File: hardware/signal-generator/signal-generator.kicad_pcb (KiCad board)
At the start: 2 copper layers, 96.6 x 92.2 mm, 68 parts, among them J1 AVR-ISP-6, J2 Conn_01x04_Male, J3 Power_Supply_Rails, J4 Conn_Coaxial, J5 Conn_01x04, SW1 RESET_BUTTON, SW2 START/STOP, SW3 MODE_SELECT, SW4 UP_ARROW, SW5 DOWN_ARROW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

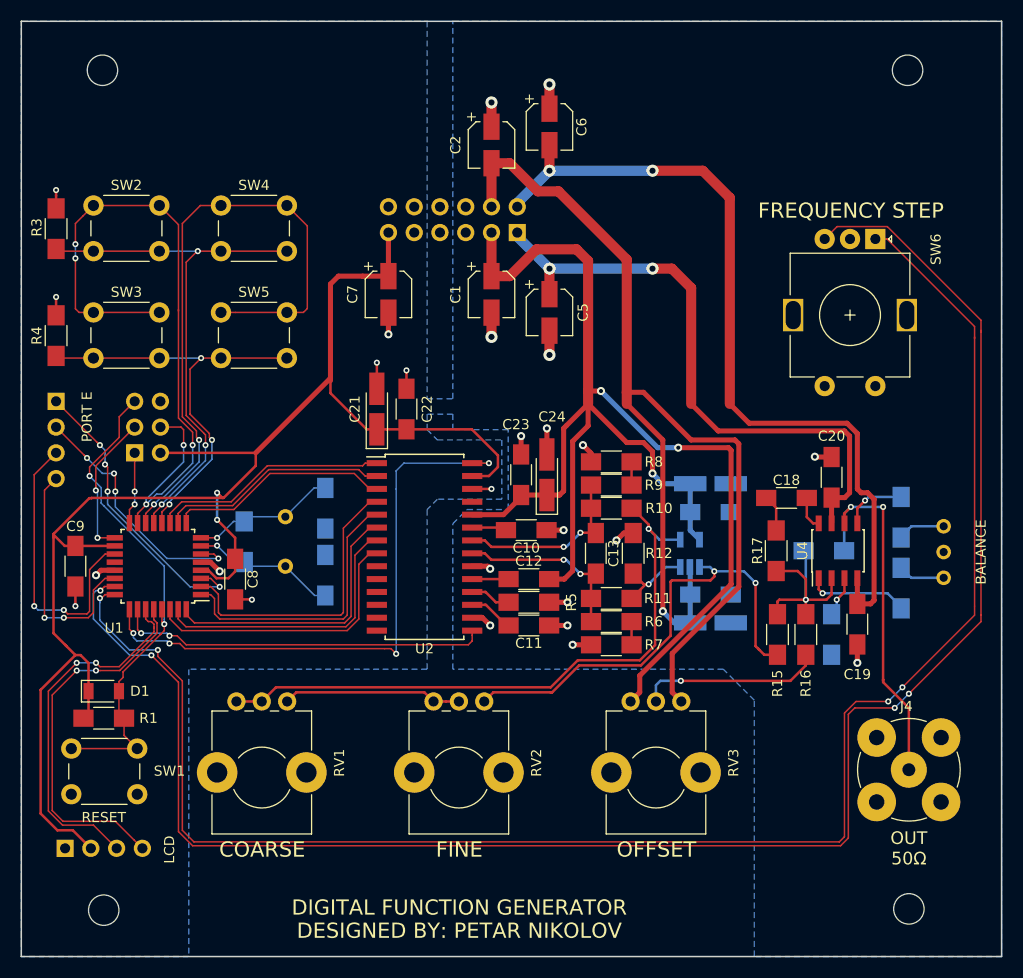
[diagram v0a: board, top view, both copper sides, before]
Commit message: [Signal Generator] Layout new amplifier on PCB
The newer amplifier's components have been placed while following the
AD8021's datasheet recommendations as well as general PCB design
guidelines. However, this is not the final PCB layout: further
fine-tuning may be applied.
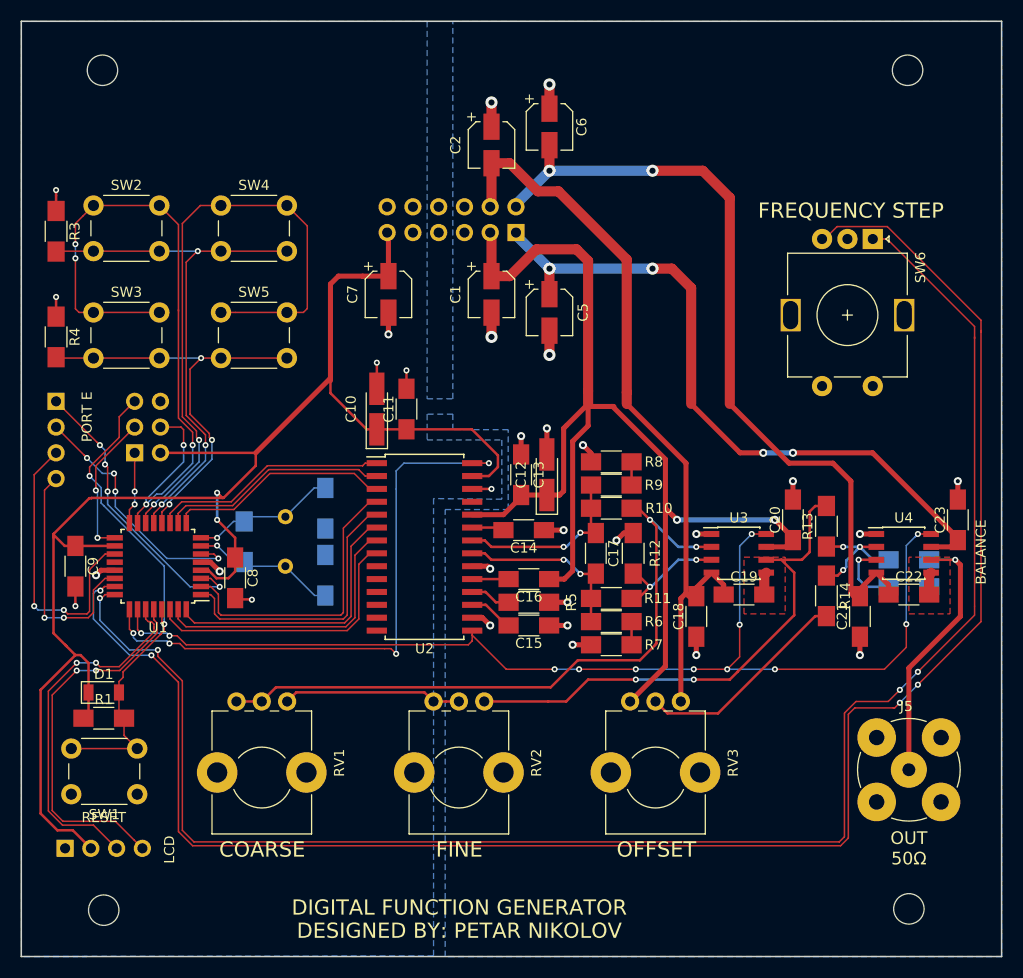
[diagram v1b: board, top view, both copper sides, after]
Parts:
- removed C24: 100nF, Capacitors_SMD:C_1206_HandSoldering
- removed R17, R19: 3k, Resistors_SMD:R_1206_HandSoldering
- removed R18: 1k5, Resistors_SMD:R_1206_HandSoldering
- removed RV4: 2k2, Potentiometers:Potentiometer_Trimmer_Bourns_3296W
- C10, C12: value 100nF -> 10uF/16V; footprint Capacitors_SMD:C_1206_HandSoldering -> Capacitors_Tantalum_SMD:CP_Tantalum_Case-A_EIA-3216-18_Hand
- C13: value 2.2nF -> 100nF
- C14: value 4.7uF/16V -> 100nF; footprint Capacitors_Tantalum_SMD:CP_Tantalum_Case-A_EIA-3216-18_Hand -> Capacitors_SMD:C_1206_HandSoldering; moved to F.Cu
- C15, C16: value 100pF -> 100nF; moved to F.Cu
- C17: value 4.7uF/16V -> 2.2nF; footprint Capacitors_Tantalum_SMD:CP_Tantalum_Case-A_EIA-3216-18_Hand -> Capacitors_SMD:C_1206_HandSoldering; moved to F.Cu
- C19, C22: value 100nF -> 6.8pF
- C21, C23: value 10uF/16V -> 100nF; footprint Capacitors_Tantalum_SMD:CP_Tantalum_Case-A_EIA-3216-18_Hand -> Capacitors_SMD:C_1206_HandSoldering
- J2: value Conn_01x04_Male -> LCD_Connector
- J3: value Power_Supply_Rails -> PORT_E; footprint Pin_Headers:Pin_Header_Straight_2x06_Pitch2.54mm -> Pin_Headers:Pin_Header_Straight_1x04_Pitch2.54mm
- J4: value Conn_Coaxial -> Power_Supply_Rails; footprint Connectors:bnc-ci -> Pin_Headers:Pin_Header_Straight_2x06_Pitch2.54mm; moved to B.Cu
- J5: value Conn_01x04 -> Output_Connector; footprint Pin_Headers:Pin_Header_Straight_1x04_Pitch2.54mm -> Connectors:bnc-ci; moved to F.Cu
- R13, R14: value 27k -> 3k; moved to F.Cu
- R15: value 3k -> 1k5; moved to B.Cu
- R16: moved to B.Cu
- U3: value TSH80 -> AD8021ARZ; footprint TO_SOT_Packages_SMD:SOT-23-5_HandSoldering -> Housings_SOIC:SOIC-8_3.9x4.9mm_Pitch1.27mm; moved to F.Cu
- U4: value LM318M -> AD8021ARZ
- moved J5 91.6 mm to (194.2, 133.9), turned to 0 degrees
- moved J4 65.6 mm to (155.4, 80.9), turned to 90 degrees
- moved C22 52.8 mm to (194.2, 116.6), turned to 0 degrees
- moved C21 51.8 mm to (189.4, 118.7)
- moved J3 48.4 mm to (110.1, 97.5), turned to 180 degrees
- moved C23 40.8 mm to (199.0, 109.2)
- moved C11 24.5 mm to (144.7, 98.3), turned to 90 degrees
- moved C14 20.6 mm to (156.2, 110.2)
- moved C16 19.1 mm to (156.7, 115.1)
- moved C10 19.0 mm to (141.7, 98.3), turned to 90 degrees
- moved C15 18.2 mm to (156.7, 119.6)
- moved C18 14.7 mm to (173.2, 118.7), turned to 90 degrees
- moved R15 13.8 mm to (194.2, 115.8), turned to 0 degrees
- moved C17 13.2 mm to (163.3, 112.5), turned to 270 degrees
- moved R16 12.5 mm to (194.2, 113.2), turned to 180 degrees
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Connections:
- C10 pad 1: AGND -> +5VD
- C10 pad 2: Net-(C10-Pad2) -> AGND
- C11 pad 1: AGND -> +5VD
- C11 pad 2: Net-(C11-Pad2) -> AGND
- C12 pad 2: Net-(C12-Pad2) -> AGND
- C13 pad 1: /Output_Circuitry/IINA -> AGND
- C13 pad 2: /Output_Circuitry/IINB -> +5VA
- C14 pad 2: -5VA -> Net-(C14-Pad2)
- C15 pad 2: -5VA -> Net-(C15-Pad2)
- C16 pad 1: AGND -> +5VA
- C16 pad 2: +5VA -> Net-(C16-Pad2)
- C17 pad 1: +5VA -> /Output_Circuitry/IINA
- C17 pad 2: AGND -> /Output_Circuitry/IINB
- C18 pad 1: Net-(C18-Pad1) -> AGND
- C18 pad 2: /Output_Circuitry/COMP -> -5VA
- C19 pad 1: AGND -> -5VA
- C19 pad 2: -12VA -> Net-(C19-Pad2)
- C20 pad 1: AGND -> +5VA
- C20 pad 2: +12VA -> AGND
- C21 pad 1: +5VD -> AGND
- C21 pad 2: AGND -> -12VA
- C22 pad 1: +5VD -> -12VA
- C22 pad 2: AGND -> Net-(C22-Pad2)
- C23 pad 1: +5VA -> +12VA
- J3 pad 1: +12VA -> Net-(J3-Pad1)
- J3 pad 2: -12VA -> Net-(J3-Pad2)
- J3 pad 3: +5VA -> Net-(J3-Pad3)
- J3 pad 4: -5VA -> Net-(J3-Pad4)
- J4 pad 1: /Output_Circuitry/VOUT -> +12VA
- J4 pad 2: AGND -> -12VA
- J5 pad 1: Net-(J5-Pad1) -> /Output_Circuitry/VOUT
- J5 pad 2: Net-(J5-Pad2) -> AGND
- R13 pad 1: /Output_Circuitry/BAL1 -> Net-(R13-Pad1)
- R14 pad 1: /Output_Circuitry/BAL2 -> Net-(R13-Pad1)
- R15 pad 2: Net-(R15-Pad2) -> AGND
- R16 pad 1: Net-(R15-Pad1) -> /Output_Circuitry/VOUT
- R16 pad 2: Net-(R16-Pad2) -> Net-(R13-Pad1)
- RV2 pad 3: Net-(R15-Pad2) -> Net-(R13-Pad2)
- RV3 pad 2: Net-(R16-Pad2) -> Net-(R14-Pad2)
- U1 pad 19: Net-(J5-Pad3) -> Net-(J3-Pad3)
- U1 pad 22: Net-(J5-Pad4) -> Net-(J3-Pad4)
- U1 pad 3: Net-(J5-Pad1) -> Net-(J3-Pad1)
- U1 pad 6: Net-(J5-Pad2) -> Net-(J3-Pad2)
- U2 pad 17: Net-(C11-Pad2) -> Net-(C15-Pad2)
- U2 pad 19: Net-(C12-Pad2) -> Net-(C16-Pad2)
- U2 pad 23: Net-(C10-Pad2) -> Net-(C14-Pad2)
- U3 pad 1: Net-(R15-Pad2) -> AGND
- U3 pad 2: -5VA -> Net-(R10-Pad1)
- U3 pad 4: Net-(R10-Pad1) -> -5VA
- U3 pad 5: +5VA -> Net-(C19-Pad2)
- U4 pad 1: /Output_Circuitry/BAL1 -> AGND
- U4 pad 2: Net-(R15-Pad1) -> Net-(R13-Pad1)
- U4 pad 3: Net-(R18-Pad1) -> Net-(R15-Pad1)
- U4 pad 5: /Output_Circuitry/BAL2 -> Net-(C22-Pad2)
- U4 pad 8: /Output_Circuitry/COMP -> /DAC/SLEEP
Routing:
- net /DAC/SLEEP: track 36.8 -> 110.6 mm, vias 2 -> 12
- net Net-(R15-Pad2): track 46.5 -> 0.00 mm, vias 2 -> 0
- net Net-(R13-Pad2): track 4.60 -> 50.5 mm, vias 0 -> 2
- net -5VA: track 108.1 -> 74.7 mm, vias 1 -> 0
- net Net-(J5-Pad3): track 29.1 -> 0.00 mm, vias 2 -> 0
- net Net-(J3-Pad3): track 0.00 -> 29.1 mm, vias 0 -> 2
- net Net-(J5-Pad1): track 28.9 -> 0.00 mm, vias 4 -> 0
- net Net-(J3-Pad1): track 0.00 -> 28.9 mm, vias 0 -> 4
- net Net-(J5-Pad2): track 25.1 -> 0.00 mm, vias 4 -> 0
- net Net-(J3-Pad2): track 0.00 -> 25.1 mm, vias 0 -> 4
- net Net-(J5-Pad4): track 24.0 -> 0.00 mm, vias 2 -> 0
- net Net-(J3-Pad4): track 0.00 -> 24.0 mm, vias 0 -> 2
- net Net-(R16-Pad2): track 18.7 -> 0.00 mm, vias 1 -> 0
- net Net-(R14-Pad2): track 4.71 -> 21.3 mm
- net +5VA: track 135.5 -> 121.9 mm, vias 3 -> 2
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- added copper zone on F.Cu, net /Output_Circuitry/VOUT
- added copper zone on F.Cu, net Net-(R13-Pad2)

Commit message: [Signal Generator] Finalize newer PCB board layout
The new design is final for rev.2. In comparison to rev.1 the presented
design implements the following changes:
- The output circuitry has been redesigned from head to toe. The new
circuitry utilizes Analog Devices's AD8021 opamp. These amplifiers have
some advantages compared to the previous amplifiers: a more conventional
interface, disable functionality for power efficiency, overall better
static and dynamic characteristics;
- In comparison with the previously used opamps, the newer AD8021 opamps
require less supportive components, thus reducing the cost of the
project, as well as increasing the available board space.

Other introduced changes compared to the previous commit:
- Slightly resize the PCB (lower its width);
- Associate numerous footprints with their corresponding 3D models;
- Realign references and other texts on the "Silk" and "Fab" layers;
- Extend the ground planes down to the lower edge of the PCB. The
potentiometers are now encased by both planes.
- Optimize routing in various places.
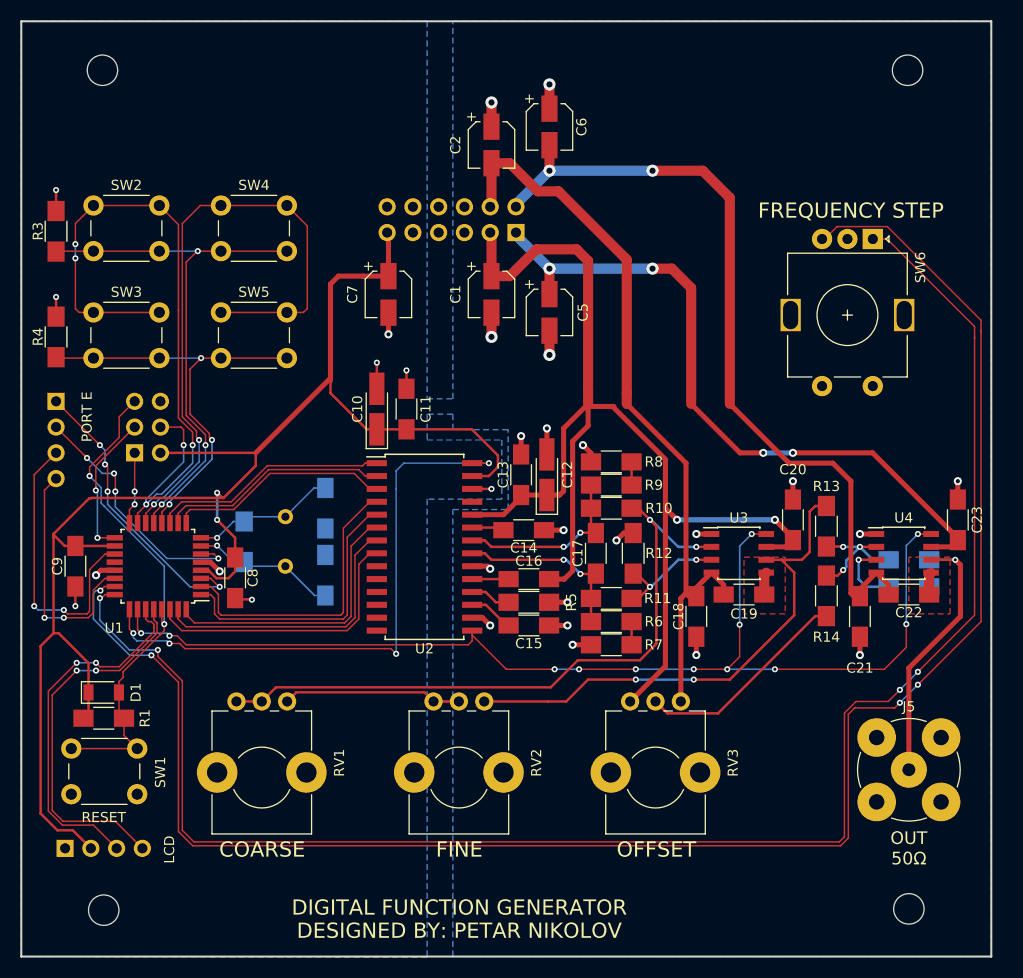
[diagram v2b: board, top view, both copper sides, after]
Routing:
- net +5VD: track 151.4 -> 152.5 mm
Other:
- board size 96.6 x 92.2 mm -> 95.6 x 92.2 mm
- board text removed: "BALANCE"
